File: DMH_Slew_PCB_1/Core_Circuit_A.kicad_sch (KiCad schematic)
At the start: 29 parts, among them Q1 BC548, Q2 BC558, Q3 BC558, Q4 BC548, SW1 SW_SPDT, SW2 SW_DPDT, U3 TL074

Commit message: Schematic design in progress
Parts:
- removed SW2: SW_DPDT, SynthStuff:Toggle_Switch_2_Poles_TE, symbol SynthStuff:Switch_DPDT
- SW1: Function (none) -> Lin / Exp
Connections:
- net A Fall Pot: now reaches R23.2
- net A Fall CV: now reaches R22.2
- net Slew A CV renamed A Rise CV
- net Slew A Pot G1 renamed A Rise Pot
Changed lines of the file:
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@@
 	)
 	(junction
-		(at 152.4 25.4)
-		(diameter 0)
-		(color 0 0 0 0)
-	)
-	(junction
 		(at 165.1 76.2)
 		(diameter 0)
@@
 	(wire
 		(pts
-			(xy 203.2 25.4) (xy 191.77 25.4)
+			(xy 203.2 38.1) (xy 177.8 38.1)
 		)
 		(stroke
@@
 	(wire
 		(pts
-			(xy 127 25.4) (xy 152.4 25.4)
+			(xy 127 38.1) (xy 152.4 38.1)
 		)
 		(stroke
@@
 	(wire
 		(pts
-			(xy 176.53 30.48) (xy 176.53 34.29)
-		)
-		(stroke
-			(width 0)
-			(type default)
-		)
-	)
-	(wire
-		(pts
-			(xy 191.77 25.4) (xy 191.77 34.29)
-		)
-		(stroke
-			(width 0)
-			(type default)
-		)
-	)
-	(wire
-		(pts
 			(xy 177.8 63.5) (xy 180.34 63.5)
 		)
@@
 	(wire
 		(pts
-			(xy 189.23 44.45) (xy 189.23 45.72)
-		)
-		(stroke
-			(width 0)
-			(type default)
-		)
-	)
-	(wire
-		(pts
 			(xy 152.4 63.5) (xy 152.4 68.58)
 		)
@@
 	(wire
 		(pts
-			(xy 190.5 45.72) (xy 189.23 45.72)
-		)
-		(stroke
-			(width 0)
-			(type default)
-		)
-	)
-	(wire
-		(pts
 			(xy 60.96 132.08) (xy 68.58 132.08)
 		)
@@
 	(wire
 		(pts
-			(xy 190.5 46.99) (xy 190.5 45.72)
+			(xy 190.5 44.45) (xy 190.5 46.99)
 		)
 		(stroke
@@
 	(wire
 		(pts
-			(xy 86.36 125.73) (xy 86.36 133.35)
+			(xy 177.8 38.1) (xy 177.8 46.99)
 		)
 		(stroke
@@
 	(wire
 		(pts
-			(xy 181.61 30.48) (xy 181.61 34.29)
+			(xy 86.36 125.73) (xy 86.36 133.35)
 		)
 		(stroke
@@
 	(wire
 		(pts
-			(xy 152.4 25.4) (xy 152.4 46.99)
+			(xy 152.4 38.1) (xy 152.4 46.99)
 		)
 		(stroke
@@
 	(wire
 		(pts
-			(xy 186.69 25.4) (xy 186.69 34.29)
-		)
-		(stroke
-			(width 0)
-			(type default)
-		)
-	)
-	(wire
-		(pts
 			(xy 139.7 123.19) (xy 139.7 130.81)
 		)
@@
 	(wire
 		(pts
-			(xy 139.7 30.48) (xy 139.7 46.99)
+			(xy 139.7 44.45) (xy 139.7 46.99)
 		)
 		(stroke
@@
 	(wire
 		(pts
-			(xy 127 30.48) (xy 139.7 30.48)
+			(xy 127 44.45) (xy 139.7 44.45)
 		)
 		(stroke
@@
 	(wire
 		(pts
-			(xy 177.8 45.72) (xy 179.07 45.72)
+			(xy 139.7 95.25) (xy 147.32 95.25)
 		)
 		(stroke
@@
 	(wire
 		(pts
-			(xy 139.7 95.25) (xy 147.32 95.25)
+			(xy 190.5 86.36) (xy 201.93 86.36)
 		)
 		(stroke
@@
 	(wire
 		(pts
-			(xy 190.5 86.36) (xy 201.93 86.36)
+			(xy 82.55 158.75) (xy 220.98 158.75)
 		)
 		(stroke
@@
 	(wire
 		(pts
-			(xy 82.55 158.75) (xy 220.98 158.75)
+			(xy 203.2 44.45) (xy 190.5 44.45)
 		)
 		(stroke
@@
 	(wire
 		(pts
-			(xy 179.07 44.45) (xy 179.07 45.72)
-		)
-		(stroke
-			(width 0)
-			(type default)
-		)
-	)
-	(wire
-		(pts
 			(xy 177.8 54.61) (xy 177.8 57.15)
 		)
@@
 	(wire
 		(pts
-			(xy 203.2 30.48) (xy 181.61 30.48)
-		)
-		(stroke
-			(width 0)
-			(type default)
-		)
-	)
-	(wire
-		(pts
-			(xy 152.4 25.4) (xy 186.69 25.4)
-		)
-		(stroke
-			(width 0)
-			(type default)
-		)
-	)
-	(wire
-		(pts
 			(xy 137.16 101.6) (xy 139.7 101.6)
 		)
@@
 	(wire
 		(pts
-			(xy 177.8 46.99) (xy 177.8 45.72)
-		)
-		(stroke
-			(width 0)
-			(type default)
-		)
-	)
-	(wire
-		(pts
 			(xy 86.36 133.35) (xy 82.55 133.35)
 		)
@@
 	(wire
 		(pts
-			(xy 171.45 30.48) (xy 176.53 30.48)
-		)
-		(stroke
-			(width 0)
-			(type default)
-		)
-	)
-	(wire
-		(pts
 			(xy 220.98 76.2) (xy 220.98 88.9)
 		)
@@
 		)
 	)
-	(hierarchical_label "Slew A Pot G1"
+	(hierarchical_label "A Rise Pot"
 		(shape input)
-		(at 127 30.48 180)
+		(at 127 44.45 180)
 		(effects
 			(font
@@
 		)
 	)
-	(hierarchical_label "Slew B CV"
+	(hierarchical_label "A Fall CV"
 		(shape input)
-		(at 203.2 25.4 0)
+		(at 203.2 38.1 0)
 		(effects
 			(font
@@
 		)
 	)
-	(hierarchical_label "Slew A CV"
-		(shape input)
-		(at 127 25.4 180)
-		(effects
-			(font
-				(size 1.27 1.27)
-			)
-			(justify right)
-		)
-	)
-	(hierarchical_label "Slew A Pot G2"
+	(hierarchical_label "A Rise CV"
 		(shape input)
-		(at 171.45 30.48 180)
+		(at 127 38.1 180)
 		(effects
 			(font
@@
 		)
 	)
-	(hierarchical_label "Slew B Pot G2"
+	(hierarchical_label "A Fall Pot"
 		(shape input)
-		(at 203.2 30.48 0)
+		(at 203.2 44.45 0)
 		(effects
 			(font
@@
 		)
 		(instances
-			(project ""
+			(project "DMH_Slew_PCB_1"
 				(path "/58f4306d-5387-4983-bb08-41a2313fd315/7ad2d702-dfb7-4d49-a82d-34430dd5948f"
 					(reference "Q1")
@@
 		)
 		(instances
-			(project ""
+			(project "DMH_Slew_PCB_1"
 				(path "/58f4306d-5387-4983-bb08-41a2313fd315/7ad2d702-dfb7-4d49-a82d-34430dd5948f"
 					(reference "#PWR021")
@@
 		)
 		(instances
-			(project ""
+			(project "DMH_Slew_PCB_1"
 				(path "/58f4306d-5387-4983-bb08-41a2313fd315/7ad2d702-dfb7-4d49-a82d-34430dd5948f"
 					(reference "U3")
@@
 		)
 		(instances
-			(project ""
+			(project "DMH_Slew_PCB_1"
 				(path "/58f4306d-5387-4983-bb08-41a2313fd315/7ad2d702-dfb7-4d49-a82d-34430dd5948f"
 					(reference "Q4")
@@
 		(on_board yes)
 		(dnp no)
-		(fields_autoplaced yes)
 		(property "Reference" "SW1"
 			(at 93.98 119.3799 90)
@@
 			)
 		)
+		(property "Function" "Lin / Exp"
+			(at 98.806 124.714 90)
+			(effects
+				(font
+					(size 1.27 1.27)
+					(thickness 0.254)
+					(bold yes)
+					(italic yes)
+				)
+			)
+		)
 		(pin "2"
 		)
@@
 		)
 		(instances
-			(project ""
+			(project "DMH_Slew_PCB_1"
 				(path "/58f4306d-5387-4983-bb08-41a2313fd315/7ad2d702-dfb7-4d49-a82d-34430dd5948f"
 					(reference "SW1")
@@
 		)
 		(instances
-			(project ""
+			(project "DMH_Slew_PCB_1"
 				(path "/58f4306d-5387-4983-bb08-41a2313fd315/7ad2d702-dfb7-4d49-a82d-34430dd5948f"
 					(reference "Q2")
@@
 	)
 	(symbol
-		(lib_id "SynthStuff:Switch_DPDT")
-		(at 184.15 39.37 90)
-		(unit 1)
-		(exclude_from_sim no)
-		(in_bom yes)
-		(on_board yes)
-		(dnp no)
-		(property "Reference" "SW2"
-			(at 170.18 39.37 0)
-			(effects
-				(font
-					(size 1.27 1.27)
-				)
-			)
-		)
-		(property "Value" "SW_DPDT"
-			(at 172.72 39.37 0)
-			(effects
-				(font
-					(size 1.27 1.27)
-				)
-			)
-		)
-		(property "Footprint" "SynthStuff:Toggle_Switch_2_Poles_TE"
-			(at 179.07 39.37 0)
-			(effects
-				(font
-					(size 1.27 1.27)
-				)
-				(hide yes)
-			)
-		)
-		(property "Datasheet" "~"
-			(at 179.07 39.37 0)
-			(effects
-				(font
-					(size 1.27 1.27)
-				)
-				(hide yes)
-			)
-		)
-		(property "Description" "DPDT switch, can be ON-ON or ON-OFF-ON"
-			(at 184.15 39.37 0)
-			(effects
-				(font
-					(size 1.27 1.27)
-				)
-				(hide yes)
-			)
-		)
-		(pin "4"
-		)
-		(pin "2"
-		)
-		(pin "5"
-		)
-		(pin "1"
-		)
-		(pin "3"
-		)
-		(pin "6"
-		)
-		(instances
-			(project ""
-				(path "/58f4306d-5387-4983-bb08-41a2313fd315/7ad2d702-dfb7-4d49-a82d-34430dd5948f"
-					(reference "SW2")
-					(unit 1)
-				)
-			)
-		)
-	)
-	(symbol
 		(lib_id "power:GND")
 		(at 152.4 105.41 0)
@@
 		)
 		(instances
-			(project ""
+			(project "DMH_Slew_PCB_1"
 				(path "/58f4306d-5387-4983-bb08-41a2313fd315/7ad2d702-dfb7-4d49-a82d-34430dd5948f"
 					(reference "U3")
@@
 		)
 		(instances
-			(project ""
+			(project "DMH_Slew_PCB_1"
 				(path "/58f4306d-5387-4983-bb08-41a2313fd315/7ad2d702-dfb7-4d49-a82d-34430dd5948f"
 					(reference "#PWR05")
@@
 		)
 		(instances
-			(project ""
+			(project "DMH_Slew_PCB_1"
 				(path "/58f4306d-5387-4983-bb08-41a2313fd315/7ad2d702-dfb7-4d49-a82d-34430dd5948f"
 					(reference "U3")
@@
 		)
 		(instances
-			(project ""
+			(project "DMH_Slew_PCB_1"
 				(path "/58f4306d-5387-4983-bb08-41a2313fd315/7ad2d702-dfb7-4d49-a82d-34430dd5948f"
 					(reference "Q3")

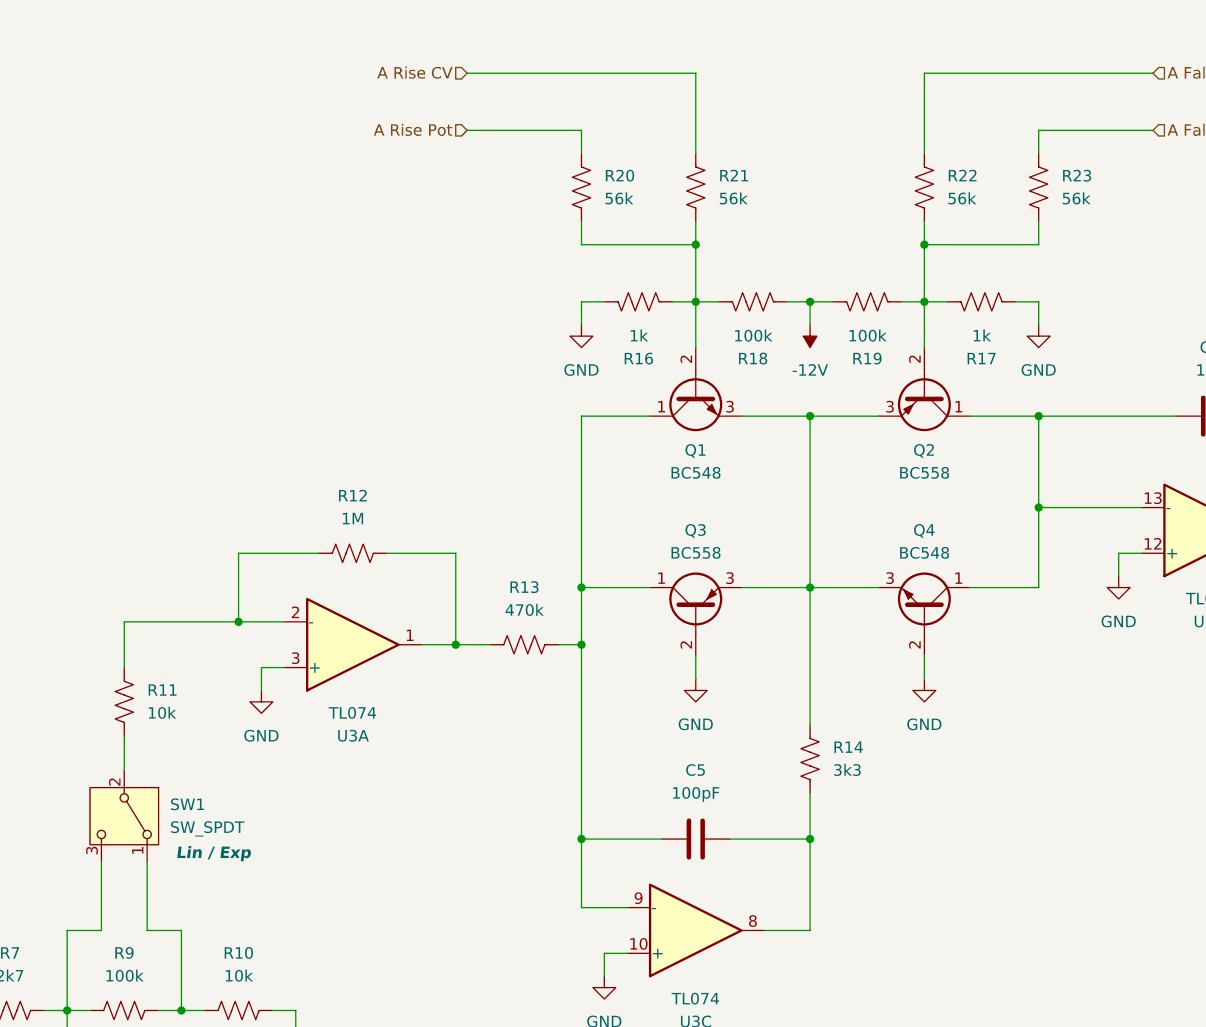
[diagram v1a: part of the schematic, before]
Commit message: Applied 10V to pots
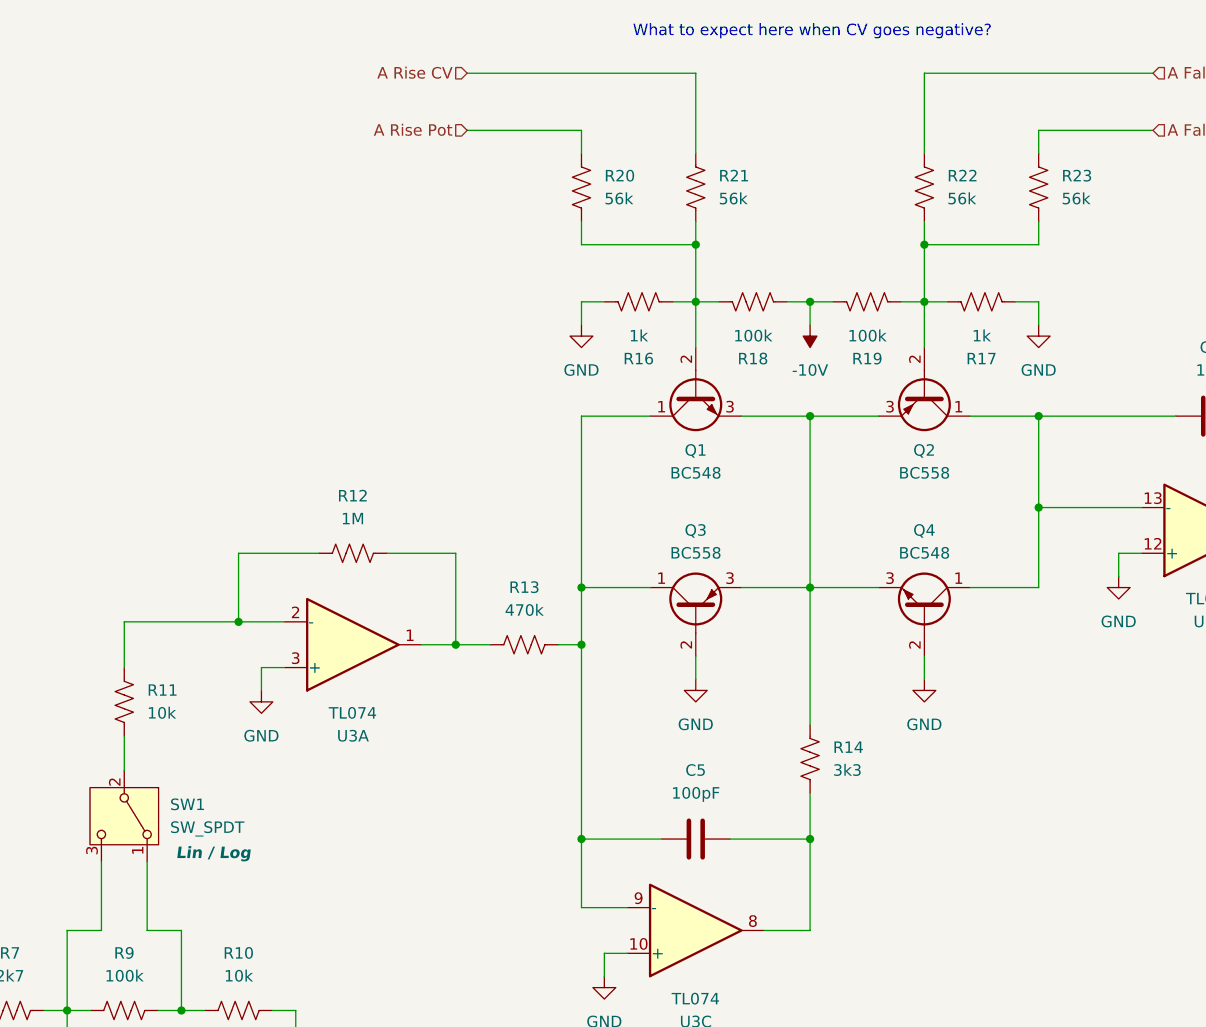
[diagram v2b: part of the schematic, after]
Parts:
- SW1: Function Lin / Exp -> Lin / Log
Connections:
- net -12V renamed -10V
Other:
- note added: "What to expect here when CV goes negative?"
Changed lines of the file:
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@@
 		(comment 1 "PCB for 5 cm Kosmo format synthesizer module")
 	)
+	(text "What to expect here when CV goes negative?"
+		(exclude_from_sim no)
+		(at 165.354 33.528 0)
+		(effects
+			(font
+				(size 1.27 1.27)
+			)
+		)
+	)
 	(junction
 		(at 165.1 123.19)
@@
 	)
 	(symbol
-		(lib_id "power:-12V")
-		(at 165.1 66.04 180)
-		(unit 1)
-		(exclude_from_sim no)
-		(in_bom yes)
-		(on_board yes)
-		(dnp no)
-		(fields_autoplaced yes)
-		(property "Reference" "#PWR021"
-			(at 165.1 62.23 0)
-			(effects
-				(font
-					(size 1.27 1.27)
-				)
-				(hide yes)
-			)
-		)
-		(property "Value" "-12V"
-			(at 165.1 71.12 0)
-			(effects
-				(font
-					(size 1.27 1.27)
-				)
-			)
-		)
-		(property "Footprint" ""
-			(at 165.1 66.04 0)
-			(effects
-				(font
-					(size 1.27 1.27)
-				)
-				(hide yes)
-			)
-		)
-		(property "Datasheet" ""
-			(at 165.1 66.04 0)
-			(effects
-				(font
-					(size 1.27 1.27)
-				)
-				(hide yes)
-			)
-		)
-		(property "Description" "Power symbol creates a global label with name \"-12V\""
-			(at 165.1 66.04 0)
-			(effects
-				(font
-					(size 1.27 1.27)
-				)
-				(hide yes)
-			)
-		)
-		(pin "1"
-		)
-		(instances
-			(project "DMH_Slew_PCB_1"
-				(path "/58f4306d-5387-4983-bb08-41a2313fd315/7ad2d702-dfb7-4d49-a82d-34430dd5948f"
-					(reference "#PWR021")
-					(unit 1)
-				)
-			)
-		)
-	)
-	(symbol
 		(lib_id "Device:R_US")
 		(at 158.75 63.5 90)
@@
 			)
 		)
-		(property "Function" "Lin / Exp"
+		(property "Function" "Lin / Log"
 			(at 98.806 124.714 90)
 			(effects
@@
 					(unit 1)
 				)
+			)
+		)
+	)
+	(symbol
+		(lib_id "power:-10V")
+		(at 165.1 66.04 180)
+		(unit 1)
+		(exclude_from_sim no)
+		(in_bom yes)
+		(on_board yes)
+		(dnp no)
+		(fields_autoplaced yes)
+		(property "Reference" "#PWR021"
+			(at 165.1 62.23 0)
+			(effects
+				(font
+					(size 1.27 1.27)
+				)
+				(hide yes)
+			)
+		)
+		(property "Value" "-10V"
+			(at 165.1 71.12 0)
+			(effects
+				(font
+					(size 1.27 1.27)
+				)
+			)
+		)
+		(property "Footprint" ""
+			(at 165.1 66.04 0)
+			(effects
+				(font
+					(size 1.27 1.27)
+				)
+				(hide yes)
+			)
+		)
+		(property "Datasheet" ""
+			(at 165.1 66.04 0)
+			(effects
+				(font
+					(size 1.27 1.27)
+				)
+				(hide yes)
+			)
+		)
+		(property "Description" "Power symbol creates a global label with name \"-10V\""
+			(at 165.1 66.04 0)
+			(effects
+				(font
+					(size 1.27 1.27)
+				)
+				(hide yes)
+			)
+		)
+		(pin "1"
+		)
+		(instances
+			(project ""
+				(path "/58f4306d-5387-4983-bb08-41a2313fd315/7ad2d702-dfb7-4d49-a82d-34430dd5948f"
+					(reference "#PWR021")
+					(unit 1)
+				)

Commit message: Exported preliminary BoM
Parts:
- SW1: footprint (none) -> SynthStuff:Toggle_Switch_TE
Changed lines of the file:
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@@
 			)
 		)
-		(property "Footprint" ""
+		(property "Footprint" "SynthStuff:Toggle_Switch_TE"
 			(at 88.9 120.65 0)
 			(effects

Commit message: Notes during breadboarding
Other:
- note added: "2k2 in breadboard"
- note added: "51k in breadboard"
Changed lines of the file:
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@@
 		(comment 1 "PCB for 5 cm Kosmo format synthesizer module")
+	)
+	(circle
+		(center 76.454 139.192)
+		(radius 5.08)
+		(stroke
+			(width 0)
+			(type default)
+		)
+		(fill
+			(type none)
+		)
+	)
+	(circle
+		(center 45.72 152.4)
+		(radius 5.08)
+		(stroke
+			(width 0)
+			(type default)
+		)
+		(fill
+			(type none)
+		)
+	)
+	(rectangle
+		(start 135.89 45.72)
+		(end 199.39 55.88)
+		(stroke
+			(width 0)
+			(type default)
+		)
+		(fill
+			(type none)
+		)
+	)
+	(circle
+		(center 83.82 152.4)
+		(radius 5.08)
+		(stroke
+			(width 0)
+			(type default)
+		)
+		(fill
+			(type none)
+		)
 	)
 	(text "What to expect here when CV goes negative?"
@@
 		(effects
 			(font
+				(size 1.27 1.27)
+			)
+		)
+	)
+	(text "2k2 in breadboard"
+		(exclude_from_sim no)
+		(at 71.882 146.304 0)
+		(effects
+			(font
+				(size 1.27 1.27)
+			)
+		)
+	)
+	(text "51k in breadboard"
+		(exclude_from_sim no)
+		(at 165.608 44.704 0)
+		(effects
+			(font
+				(size 1.27 1.27)
+			)
+		)
+	)
+	(text "51k in breadboard"
+		(exclude_from_sim no)
+		(at 56.896 159.258 0)
+		(effects
+			(font

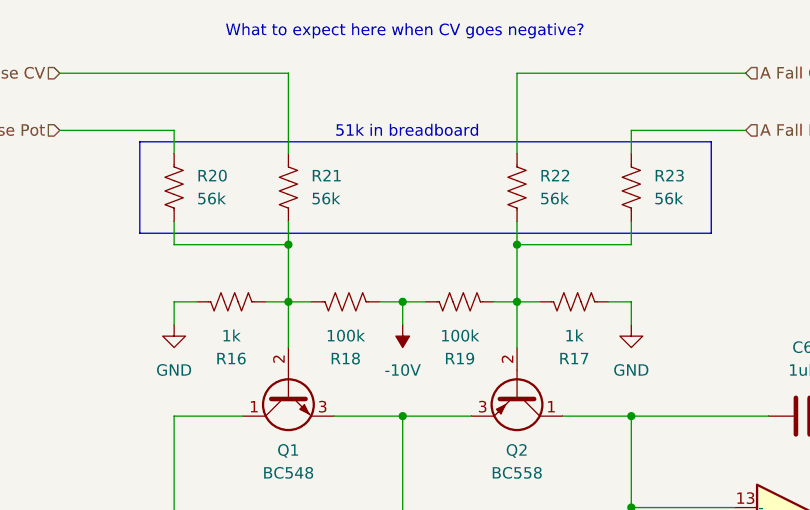
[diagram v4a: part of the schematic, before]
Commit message: Simulated core circuit
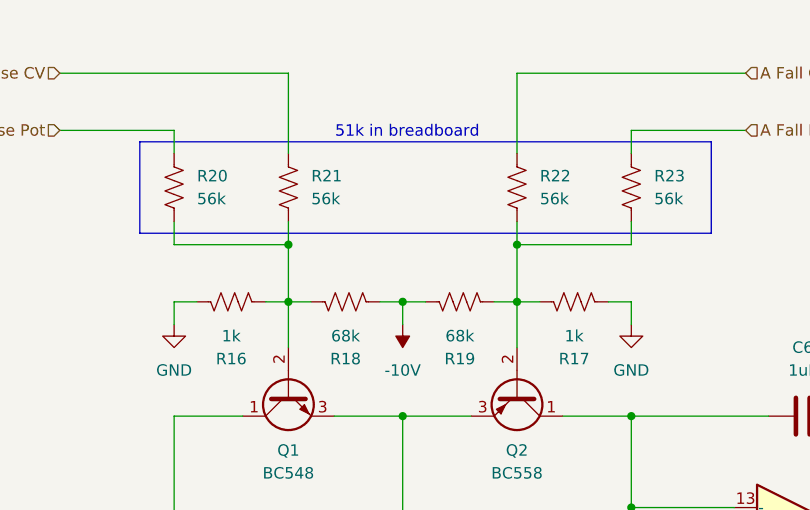
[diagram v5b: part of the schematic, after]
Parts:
- R18, R19: value 100k -> 68k
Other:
- note removed: "What to expect here when CV goes negative?"
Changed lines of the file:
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@@
-		)
-	)
-	(text "What to expect here when CV goes negative?"
-		(exclude_from_sim no)
-		(at 165.354 33.528 0)
-		(effects
-			(font
-				(size 1.27 1.27)
-			)
 		)
 	)
@@
 			)
 		)
-		(property "Value" "100k"
+		(property "Value" "68k"
 			(at 158.75 67.31 90)
 			(effects
@@
 				)
 				(hide yes)
+			)
+		)
+		(property "Function" ""
+			(at 158.75 63.5 0)
+			(effects
+				(font
+					(size 1.27 1.27)
+				)
 			)
 		)
@@
 			)
 		)
-		(property "Value" "100k"
+		(property "Value" "68k"
 			(at 171.45 67.31 90)
 			(effects
@@
 			)
 		)
+		(property "Function" ""
+			(at 171.45 63.5 0)
+			(effects
+				(font
+					(size 1.27 1.27)
+				)
+			)
+		)
